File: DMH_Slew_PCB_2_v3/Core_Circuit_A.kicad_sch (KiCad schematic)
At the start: 60 parts, among them J1 TS_Jack_6.35mm_Sw, J11 Conn_02x03_Top_Bottom, J12 Conn_02x06_Top_Bottom, J13 Conn_02x03_Top_Bottom, J14 Conn_02x03_Top_Bottom, J15 Conn_02x06_Top_Bottom, J16 Conn_02x03_Top_Bottom, J17 Conn_01x08, J18 Conn_01x08, J19 Conn_01x08, J2 TS_Jack_6.35mm_Sw, J20 Conn_01x08, J3 TS_Jack_6.35mm_Sw, Q1 BC548, Q2 BC548, Q3 BC558, Q4 BC558, SW1 SW_DPDT_3way, SW2 SW_DPDT, SW3 SPDT_OnOffOn, U1 TL074, U2 TL074

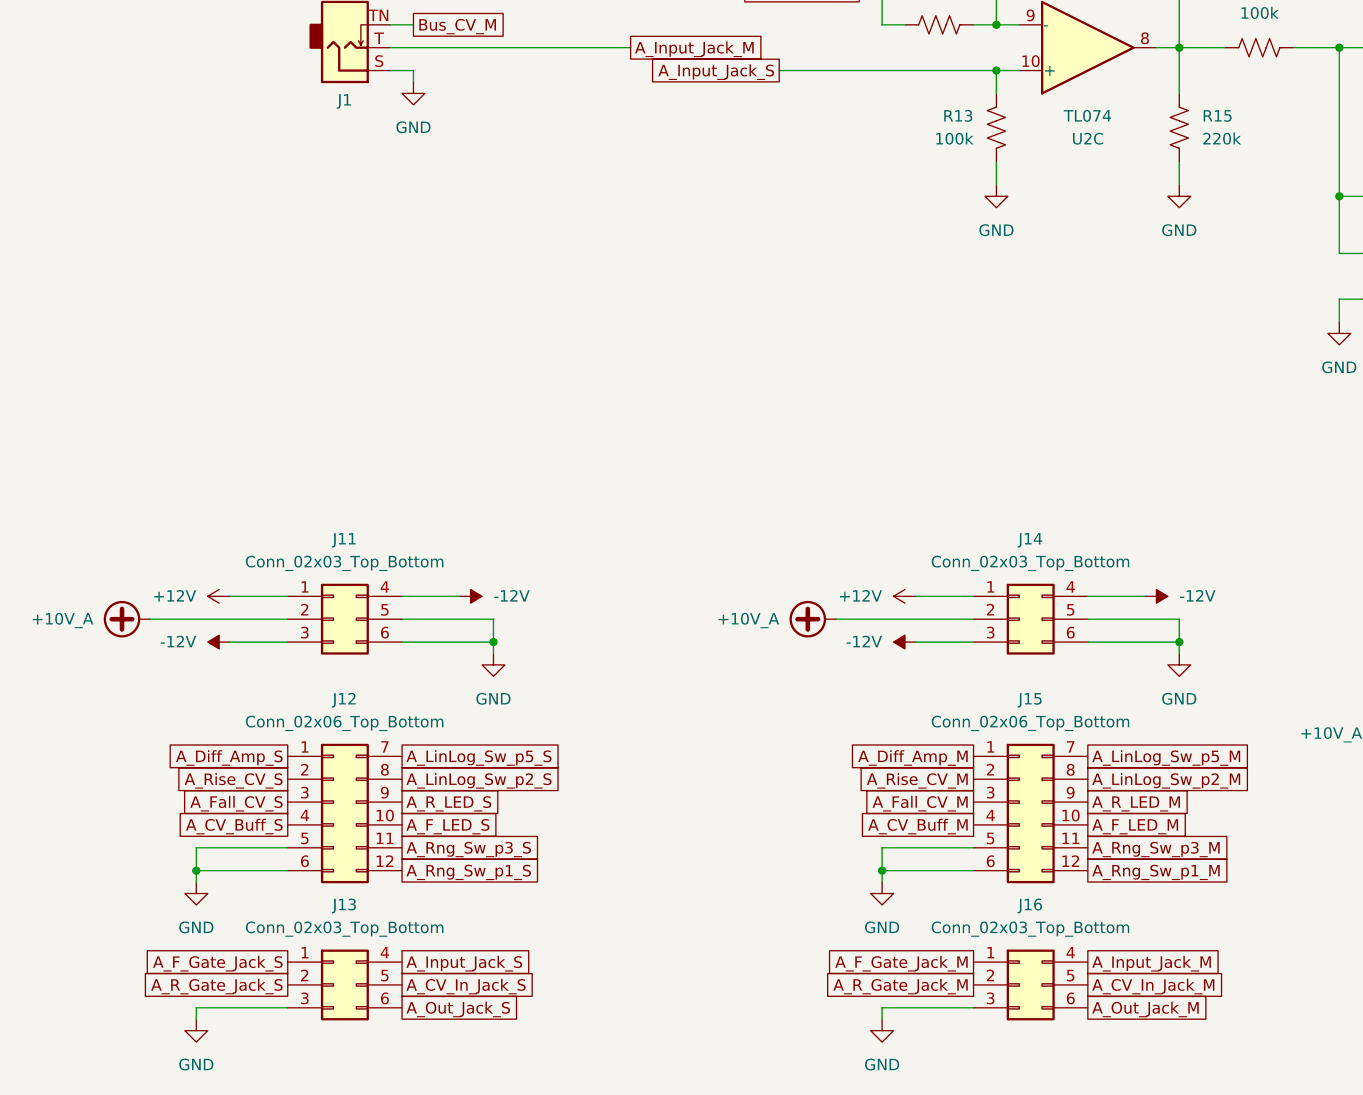
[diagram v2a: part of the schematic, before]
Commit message: Exposed loopback resistor to submodule connector
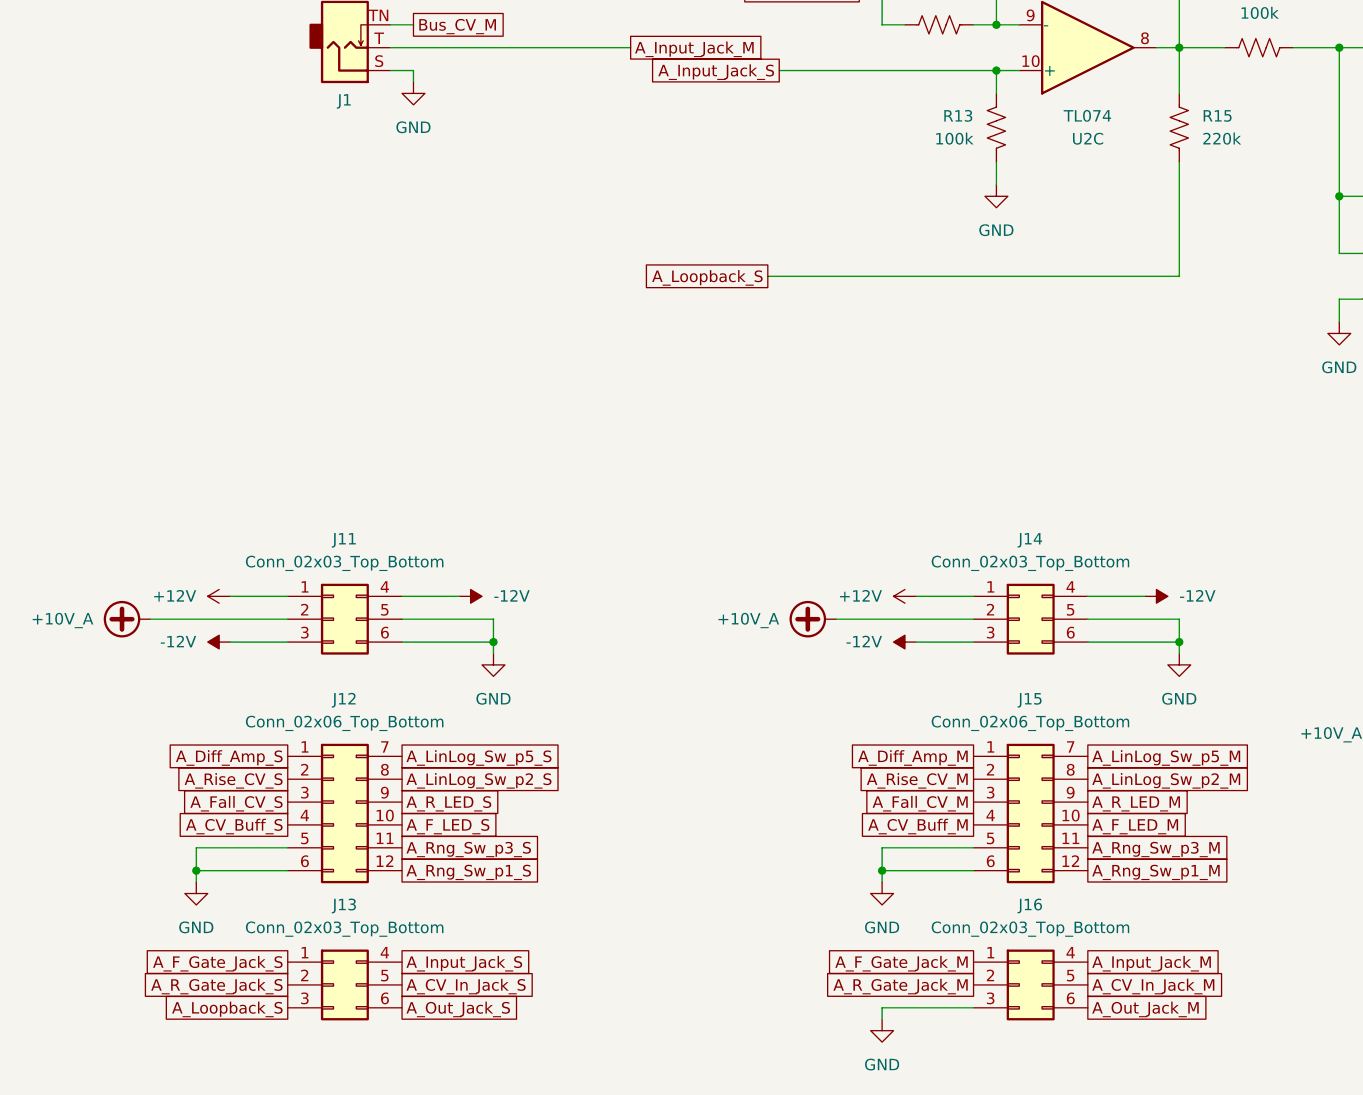
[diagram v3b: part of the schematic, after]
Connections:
- net GND: no longer J13.3 (Pin_3), R15.2
- new net A_Loopback_S: J13.3 (Pin_3), R15.2
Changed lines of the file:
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@@
 	(wire
 		(pts
+			(xy 97.79 190.5) (xy 143.51 190.5)
+		)
+		(stroke
+			(width 0)
+			(type default)
+		)
+	)
+	(wire
+		(pts
 			(xy 167.64 104.14) (xy 186.69 104.14)
 		)
@@
 	(wire
 		(pts
-			(xy 266.7 88.9) (xy 271.78 88.9)
+			(xy 143.51 177.8) (xy 143.51 190.5)
 		)
 		(stroke
@@
 	(wire
 		(pts
-			(xy 143.51 177.8) (xy 143.51 180.34)
+			(xy 266.7 88.9) (xy 271.78 88.9)
 		)
 		(stroke
@@
 	(wire
 		(pts
-			(xy 44.45 271.78) (xy 34.29 271.78)
-		)
-		(stroke
-			(width 0)
-			(type default)
-		)
-	)
-	(wire
-		(pts
 			(xy 266.7 127) (xy 266.7 123.19)
 		)
@@
 	(wire
 		(pts
-			(xy 34.29 271.78) (xy 34.29 273.05)
-		)
-		(stroke
-			(width 0)
-			(type default)
-		)
-	)
-	(wire
-		(pts
 			(xy 303.53 129.54) (xy 307.34 129.54)
 		)
@@
 		)
 	)
+	(global_label "A_Loopback_S"
+		(shape passive)
+		(at 44.45 271.78 180)
+		(fields_autoplaced yes)
+		(effects
+			(font
+				(size 1.27 1.27)
+			)
+			(justify right)
+		)
+		(property "Intersheetrefs" "${INTERSHEET_REFS}"
+			(at 29.453 271.78 0)
+			(effects
+				(font
+					(size 1.27 1.27)
+				)
+				(justify right)
+				(hide yes)
+			)
+		)
+	)
 	(global_label "A_CV_Buff_C"
 		(shape passive)
@@
 		)
 	)
+	(global_label "A_Loopback_S"
+		(shape passive)
+		(at 97.79 190.5 180)
+		(fields_autoplaced yes)
+		(effects
+			(font
+				(size 1.27 1.27)
+			)
+			(justify right)
+		)
+		(property "Intersheetrefs" "${INTERSHEET_REFS}"
+			(at 82.793 190.5 0)
+			(effects
+				(font
+					(size 1.27 1.27)
+				)
+				(justify right)
+				(hide yes)
+			)
+		)
+	)
 	(global_label "A_LinLog_Sw_p2_S"
 		(shape passive)
@@
 		(polyline
 			(pts
-				(xy 44.45 152.4) (xy 78.74 152.4) (xy 78.74 177.8) (xy 44.45 177.8)
+				(xy 45.085 152.4) (xy 79.375 152.4) (xy 79.375 198.12) (xy 45.085 198.12)
 			)
 			(stroke
@@
 		(length 2.54)
 		(shape round)
-		(at 44.45 152.4 0)
+		(at 45.72 152.4 0)
 		(fields_autoplaced yes)
 		(effects
@@
 		)
 		(property "Component Class" "Main PCB"
-			(at 45.1485 149.86 0)
+			(at 46.4185 149.86 0)
 			(effects
 				(font
@@
 	(symbol
 		(lib_id "power:GND")
-		(at 143.51 180.34 0)
-		(unit 1)
-		(exclude_from_sim no)
-		(in_bom yes)
-		(on_board no)
-		(dnp no)
-		(fields_autoplaced yes)
-		(property "Reference" "#PWR022"
-			(at 143.51 186.69 0)
-			(effects
-				(font
-					(size 1.27 1.27)
-				)
-				(hide yes)
-			)
-		)
-		(property "Value" "GND"
-			(at 143.51 185.42 0)
-			(effects
-				(font
-					(size 1.27 1.27)
-				)
-			)
-		)
-		(property "Footprint" ""
-			(at 143.51 180.34 0)
-			(effects
-				(font
-					(size 1.27 1.27)
-				)
-				(hide yes)
-			)
-		)
-		(property "Datasheet" ""
-			(at 143.51 180.34 0)
-			(effects
-				(font
-					(size 1.27 1.27)
-				)
-				(hide yes)
-			)
-		)
-		(property "Description" "Power symbol creates a global label with name \"GND\" , ground"
-			(at 143.51 180.34 0)
-			(effects
-				(font
-					(size 1.27 1.27)
-				)
-				(hide yes)
-			)
-		)
-		(pin "1"
-		)
-		(instances
-			(project "DMH_Slew_PCB_2_v3"
-				(path "/58f4306d-5387-4983-bb08-41a2313fd315/7ad2d702-dfb7-4d49-a82d-34430dd5948f"
-					(reference "#PWR022")
-					(unit 1)
-				)
-			)
-		)
-	)
-	(symbol
-		(lib_id "power:GND")
 		(at 44.45 86.36 0)
 		(unit 1)
@@
 					(unit 1)
 				)
-			)
-		)
-	)
-	(symbol
-		(lib_id "power:GND")
-		(at 34.29 273.05 0)
-		(mirror y)
-		(unit 1)
-		(exclude_from_sim no)
-		(in_bom yes)
-		(on_board no)
-		(dnp no)
-		(fields_autoplaced yes)
-		(property "Reference" "#PWR0101"
-			(at 34.29 279.4 0)
-			(effects
-				(font
-					(size 1.27 1.27)
-				)
-				(hide yes)
-			)
-		)
-		(property "Value" "GND"
-			(at 34.29 278.13 0)
-			(effects
-				(font
-					(size 1.27 1.27)
-				)
-			)
-		)
-		(property "Footprint" ""
-			(at 34.29 273.05 0)
-			(effects
-				(font
-					(size 1.27 1.27)
-				)
-				(hide yes)
-			)
-		)
-		(property "Datasheet" ""
-			(at 34.29 273.05 0)
-			(effects
-				(font
-					(size 1.27 1.27)
-				)
-				(hide yes)
-			)
-		)
-		(property "Description" "Power symbol creates a global label with name \"GND\" , ground"
-			(at 34.29 273.05 0)
-			(effects
-				(font
-					(size 1.27 1.27)
-				)
-				(hide yes)
-			)
-		)
-		(pin "1"
-		)
-		(instances
-			(project "DMH_Slew_PCB_2_v3"
-				(path "/58f4306d-5387-4983-bb08-41a2313fd315/7ad2d702-dfb7-4d49-a82d-34430dd5948f"
-					(reference "#PWR0101")
-					(unit 1)
-				)

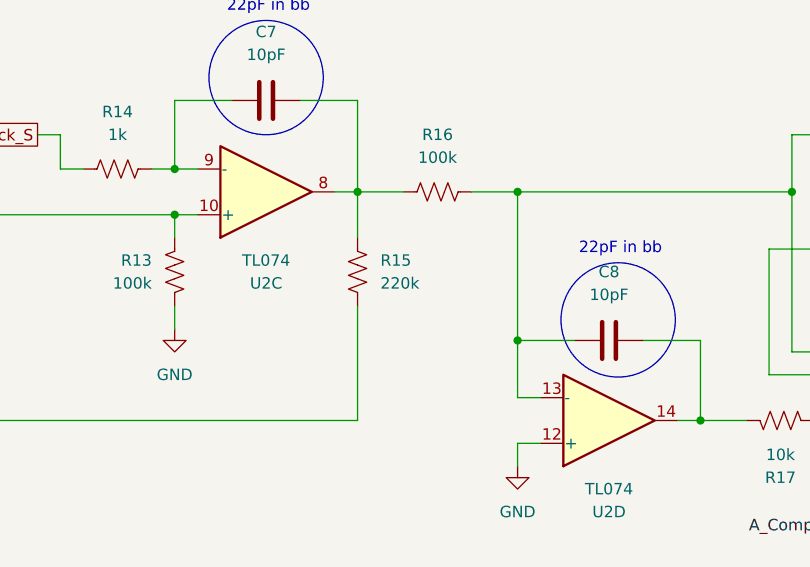
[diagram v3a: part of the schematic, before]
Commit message: Changed loopback resistor to 82k
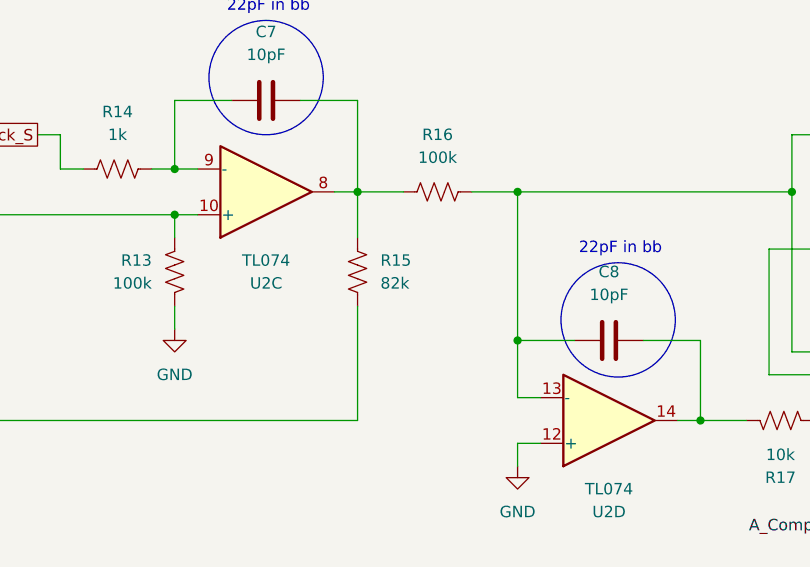
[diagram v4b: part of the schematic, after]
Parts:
- R15: value 220k -> 82k
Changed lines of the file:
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@@
 			)
 		)
-		(property "Value" "220k"
+		(property "Value" "82k"
 			(at 146.05 175.2599 0)
 			(effects
